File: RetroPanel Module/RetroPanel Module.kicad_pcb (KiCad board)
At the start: 2 copper layers, 100 x 97.9 mm, 77 parts, among them J1 Front Panel, J10 SW_EXTRA, J11 RS-232, J12 +5VSB, J13 PWR_ON, J14 PWR_OK, J15 COMMON, J16 SPEAKER, J17 LED_HDD, J2 SW_POWER, J3 LED_POWER, J4 SW_RESET, J5 SW_TURBO, J6 LED_TURBO, J7 POWER, J8 IIC, J9 POST_CARD, M1 Mounting_Pin, M10 Mounting_Pad, M11 Mounting_Pad, M12 Mounting_Pad, M13 Mounting_Pad, M14 Mounting_Pad, M15 Mounting_Pad, M16 Mounting_Pin, M2 Mounting_Pin, M3 Mounting_Pin, M5 Mounting_Pad, M7 Mounting_Pad, M8 Mounting_Pad, M9 Mounting_Pad, Q1 2N3904 *, Q2 2N3904 *, Q3 2N3904 *, Q4 2N3904 *, U1 MAX232, U2 NE555P

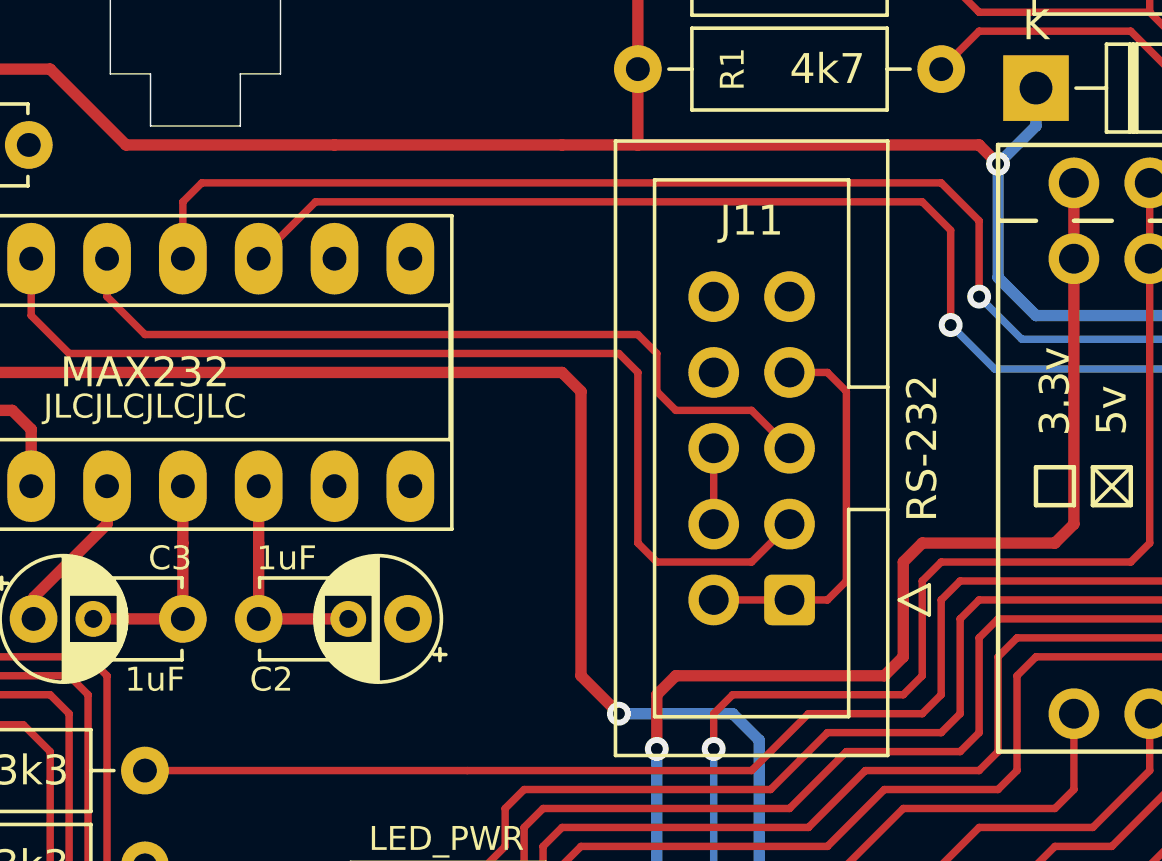
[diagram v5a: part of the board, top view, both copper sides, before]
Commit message: Add external pullup for Serial1 RX
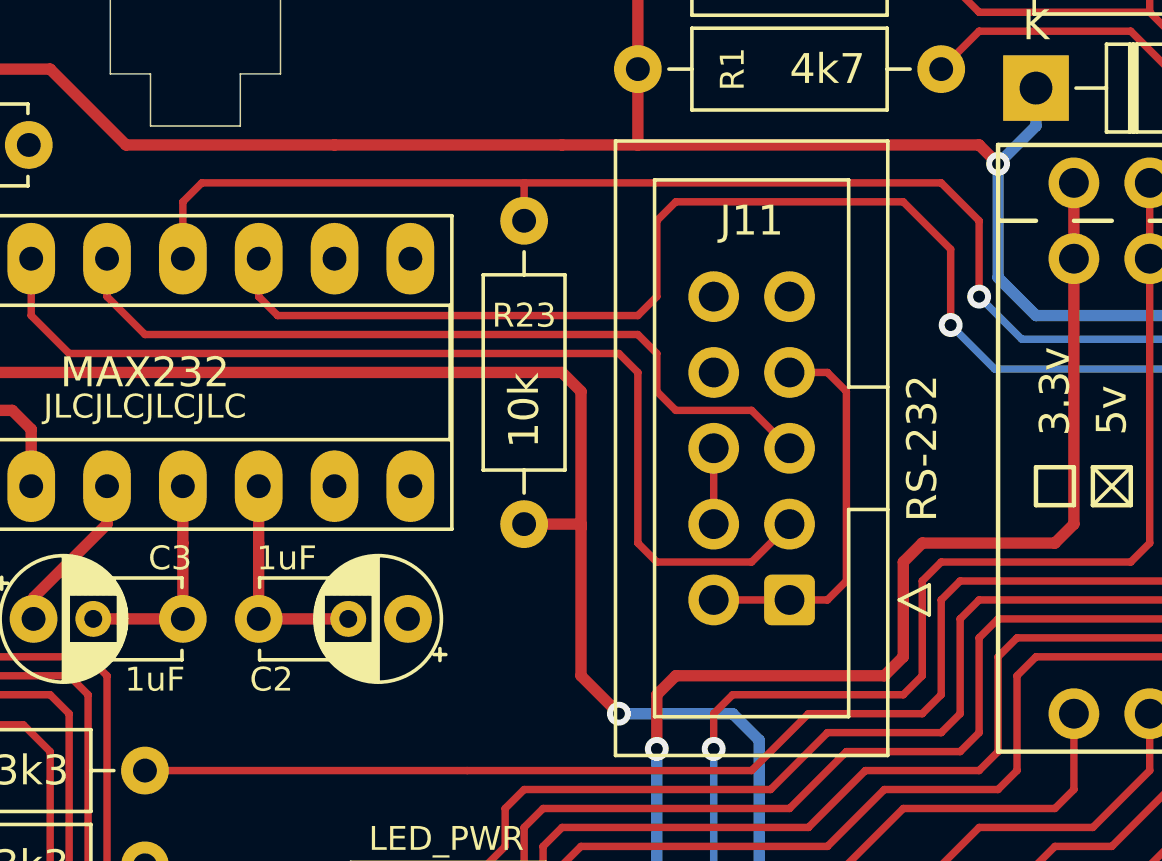
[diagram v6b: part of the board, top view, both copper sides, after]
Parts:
- added R23: 10k, resistor:R_Axial_DIN0207_L6.3mm_D2.5mm_P10.16mm_Horizontal, F.Cu at (151.2, 72.7)
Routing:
- net TTL_TX: track 65.0 -> 68.5 mm
- net +5V: track 259.8 -> 261.7 mm
- net TTL_RX: track 65.5 -> 66.7 mm

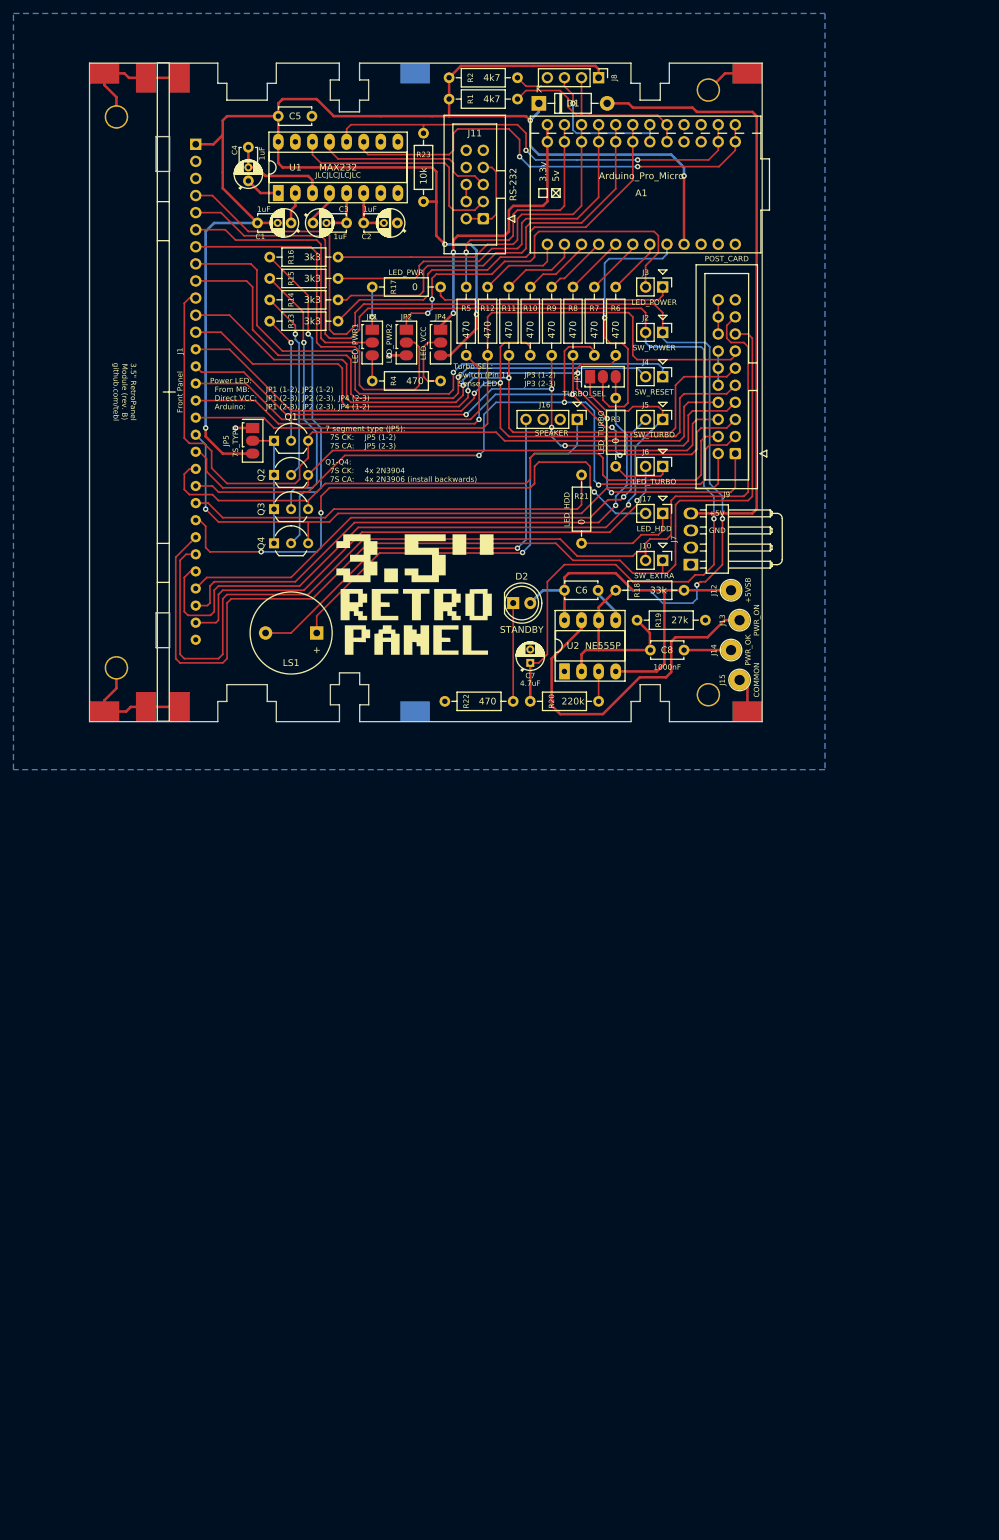
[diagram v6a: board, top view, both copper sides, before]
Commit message: Add mounting spot for DS3231 directly
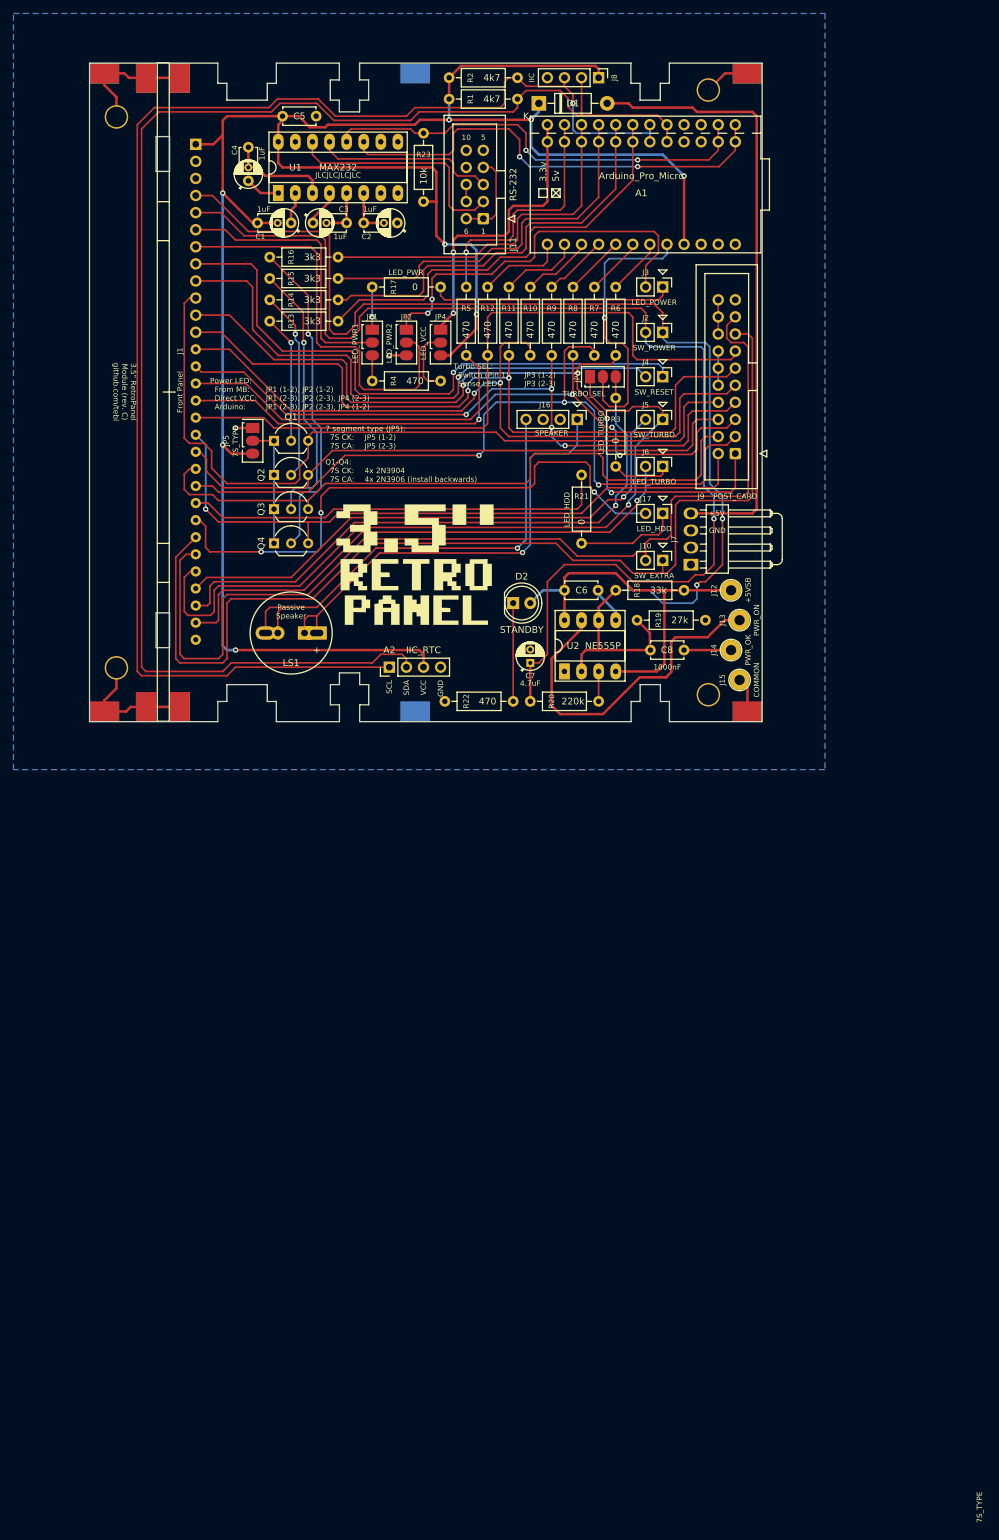
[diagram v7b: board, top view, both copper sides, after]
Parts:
- added ?: , , F.Cu at (90.3, 124.8)
- added A2: IIC_RTC, RetroPanel:DS3231_ZS-042, F.Cu at (146.2, 141.9)
- D1: value 1N4001 -> 1N5819
- LS1: value Speaker -> Passive Speaker; footprint Buzzer_Beeper:Buzzer_12x9.5RM7.6 -> small_buzzer:Buzzer_12x9.5RM7.6
- moved G*** 4.45 mm to (150.0, 126.7)
- moved C5 0.63 mm to (130.3, 60.0)
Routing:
- net IIC_SCL: track 30.0 -> 212.9 mm
- net IIC_SDA: track 33.8 -> 216.6 mm
- net +5V: track 261.7 -> 317.7 mm, vias 5 -> 8
- net Net-(J16-Pad4): track 62.3 -> 68.3 mm
- net Net-(J16-Pad1): track 63.2 -> 67.2 mm
- net TTL_RX: track 66.7 -> 65.6 mm
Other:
- board text added: "1"
- board text added: "10"
- board text added: "3.5" RetroPanel Module (rev. C) github.com/tebl"
- board text added: "5"
- board text added: "6"
- board text added: "Passive Speaker"
- board text added: "SCL"
- board text added: "SDA"
- board text added: "VCC"
- board text removed: "3.5" RetroPanel Module (rev. B) github.com/tebl"

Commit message: Adjust cutout to move unit forward
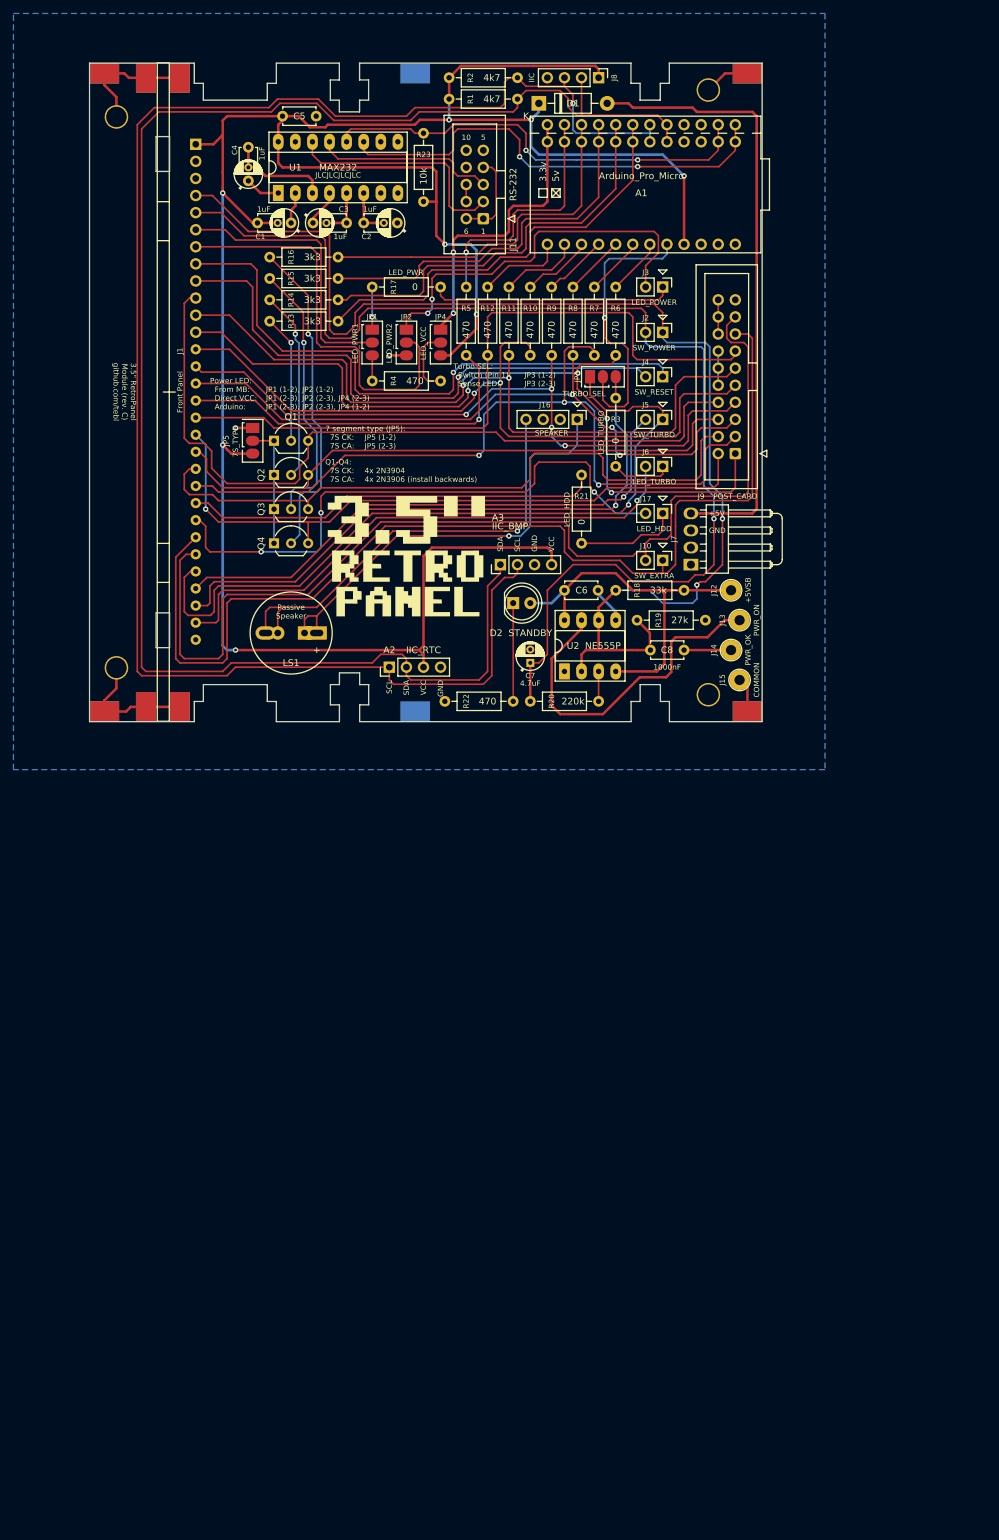
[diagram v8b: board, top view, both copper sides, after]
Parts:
- removed ?: , 
- added A3: IIC_BMP, RetroPanel:BMP280-5V, F.Cu at (162.7, 126.7)
- moved G*** 1.80 mm to (148.7, 125.4)
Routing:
- net IIC_SCL: track 212.9 -> 249.6 mm
- net +5V: track 317.7 -> 353.7 mm
- net IIC_SDA: track 216.6 -> 247.4 mm
- net SW_EXTRA1: track 157.5 -> 161.4 mm
- net SW_EXTRA2: track 152.6 -> 156.5 mm
- net Net-(J16-Pad1): track 67.2 -> 65.6 mm
- net LED_HDD1: track 63.5 -> 62.0 mm
- net Net-(J16-Pad4): track 68.3 -> 66.8 mm
- net /Smart Switch/+5VSB: track 56.9 -> 55.8 mm
- net SW_PWR2: track 179.7 -> 178.9 mm
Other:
- outline, holes or cut-outs redrawn
